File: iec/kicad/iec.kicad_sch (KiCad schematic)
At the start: 6 parts, among them J2 Conn_RIOT, J2 RESET, J3 DIN-6, U1 74LS06

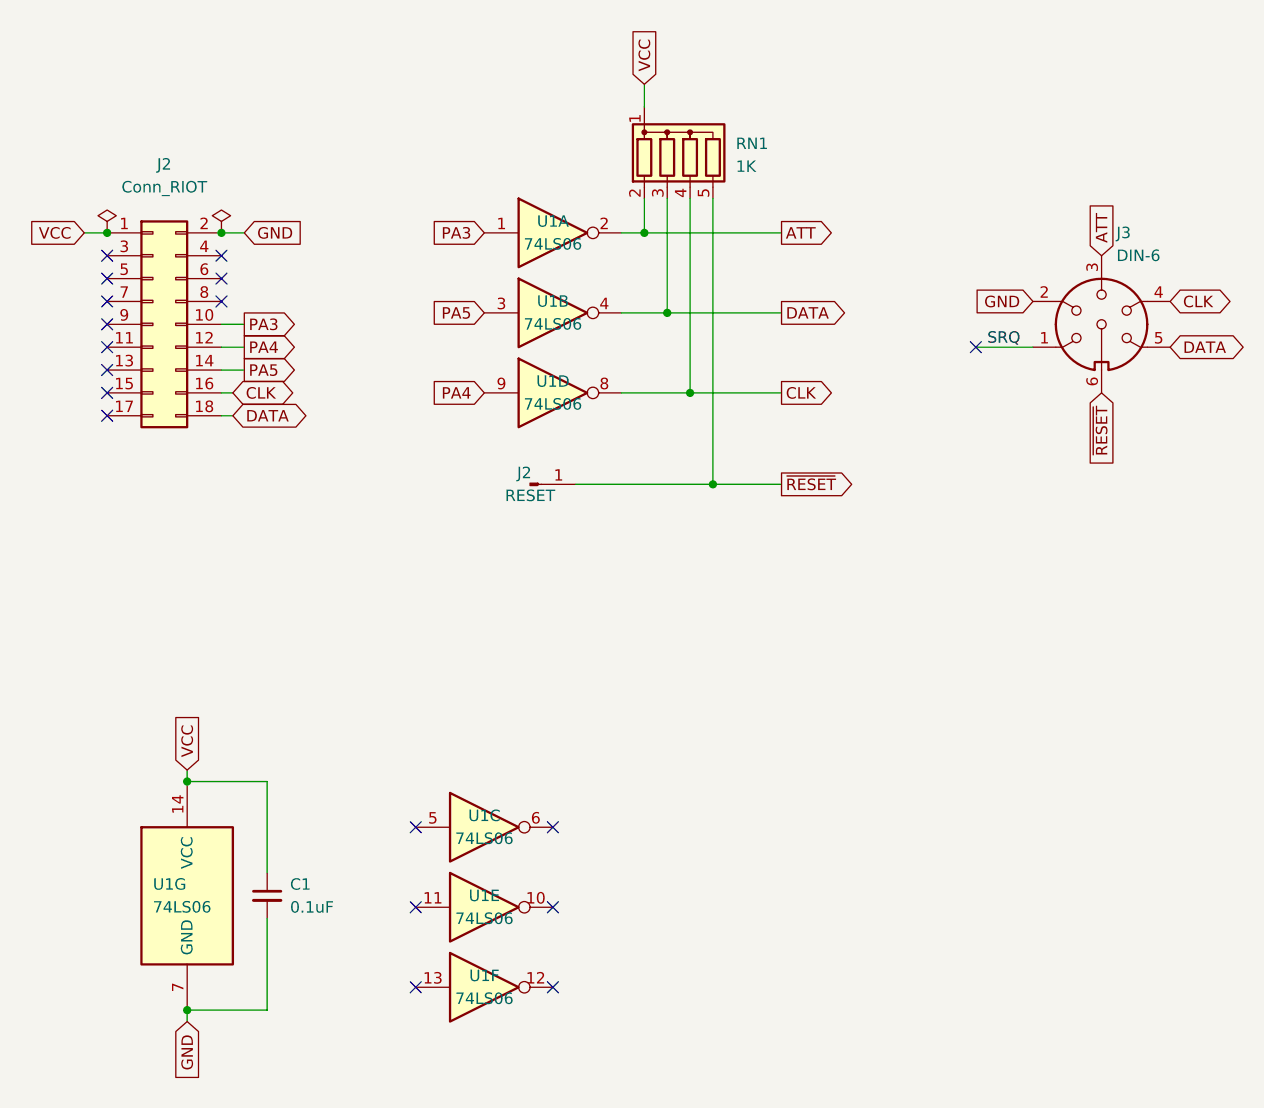
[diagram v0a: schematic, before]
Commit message: Expose VCC and GND via pins for SD2IEC devices
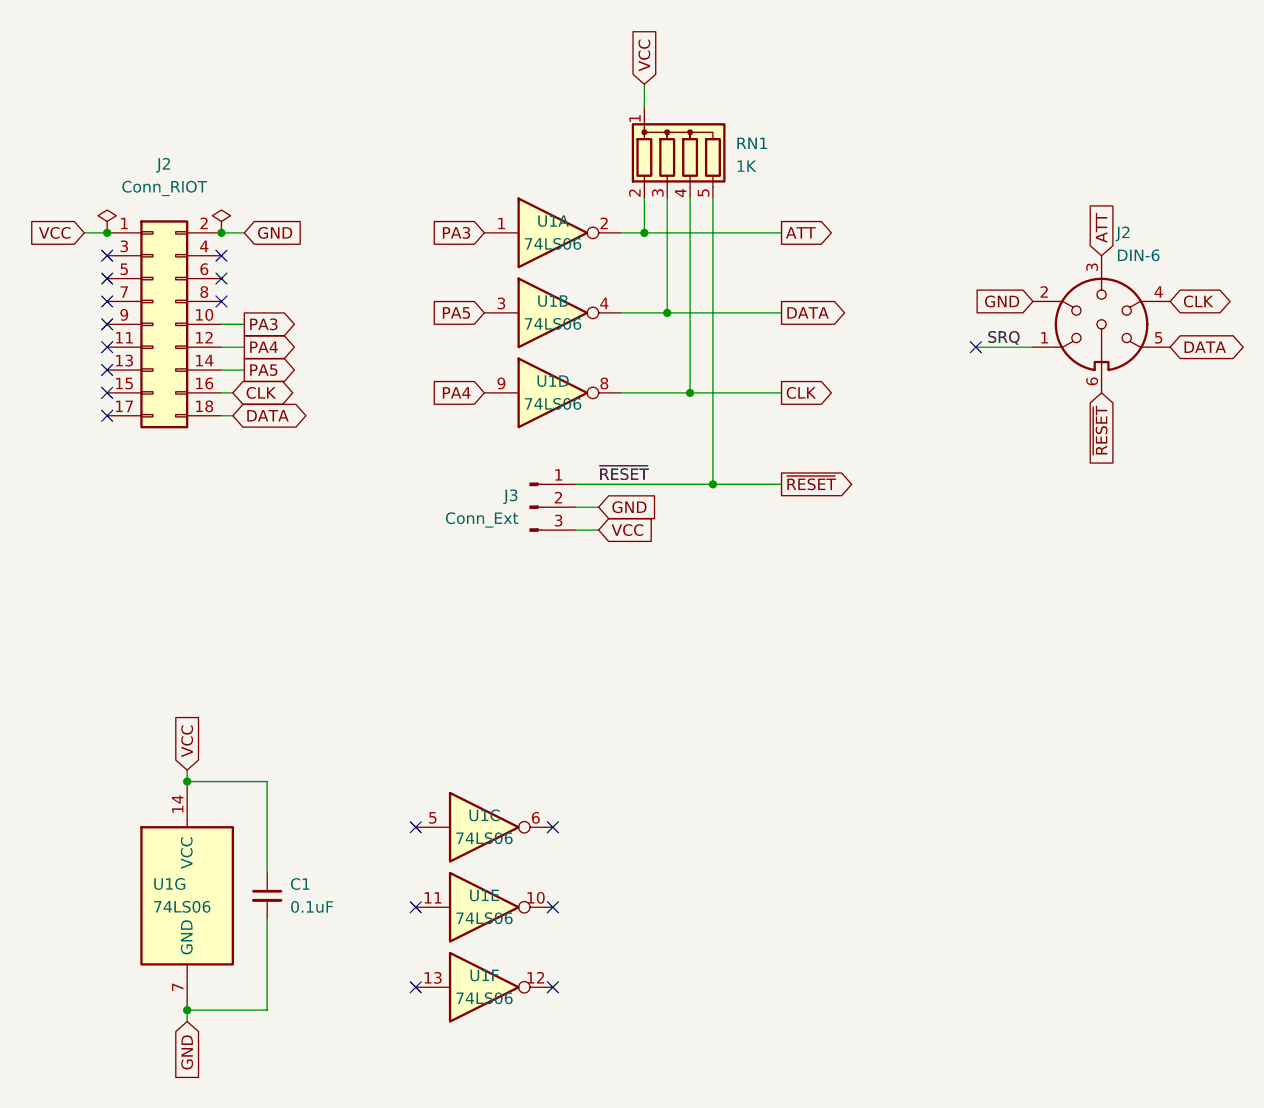
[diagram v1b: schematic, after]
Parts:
- removed J2: RESET, Connector_PinHeader_2.54mm:PinHeader_1x01_P2.54mm_Horizontal, symbol Connector:Conn_01x01_Pin
- added J3: Conn_Ext, Connector_PinHeader_2.54mm:PinHeader_1x03_P2.54mm_Vertical, symbol Connector:Conn_01x03_Pin
- renumbered J3 to J2
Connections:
- net GND: now also J3.2 (Pin_2)
- net VCC: now also J3.3 (Pin_3)
- net ~{RESET}: now also J3.1 (Pin_1)
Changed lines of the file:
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@@
+    (stroke (width 0) (type default))
+  )
+  (wire (pts (xy 151.13 102.87) (xy 148.59 102.87))
     (stroke (width 0) (type default))
   )
@@
     (stroke (width 0) (type default))
   )
+  (wire (pts (xy 151.13 105.41) (xy 148.59 105.41))
+    (stroke (width 0) (type default))
+  )
   (wire (pts (xy 105.41 133.35) (xy 114.3 133.35))
     (stroke (width 0) (type default))
+  )
+  (label "~{RESET}" (at 151.13 100.33 0) (fields_autoplaced)
+    (effects (font (size 1.27 1.27)) (justify left bottom))
   )
   (label "SRQ" (at 194.31 85.09 0) (fields_autoplaced)
@@
     )
   )
+  (global_label "VCC" (shape input) (at 151.13 105.41 0) (fields_autoplaced)
+    (effects (font (size 1.27 1.27)) (justify left))
+    (property "Intersheetrefs" "${INTERSHEET_REFS}" (at 157.6644 105.41 0)
+      (effects (font (size 1.27 1.27)) (justify left) hide)
+    )
+  )
   (global_label "PA4" (shape output) (at 111.76 85.09 0) (fields_autoplaced)
     (effects (font (size 1.27 1.27)) (justify left))
@@
     )
   )
+  (global_label "GND" (shape input) (at 151.13 102.87 0) (fields_autoplaced)
+    (effects (font (size 1.27 1.27)) (justify left))
+    (property "Intersheetrefs" "${INTERSHEET_REFS}" (at 157.9063 102.87 0)
+      (effects (font (size 1.27 1.27)) (justify left) hide)
+    )
+  )
   (symbol (lib_id "Connector:DIN-6") (at 207.01 82.55 0) (unit 1)
     (in_bom yes) (on_board yes) (dnp no) (fields_autoplaced)
-    (property "Reference" "J3" (at 208.6611 72.39 0)
+    (property "Reference" "J2" (at 208.6611 72.39 0)
       (effects (font (size 1.27 1.27)) (justify left))
     )
@@
     (pin "5")
     (pin "6")
-    (instances
-      (project "iec"
-        (path "/c75a3d49-44a2-4d4d-826f-a38b35ab1c9a"
-          (reference "J3") (unit 1)
-        )
-      )
-    )
-  )
-  (symbol (lib_id "Connector:Conn_01x01_Pin") (at 143.51 100.33 0) (unit 1)
-    (in_bom yes) (on_board yes) (dnp no)
-    (property "Reference" "J2" (at 142.875 99.06 0)
-      (effects (font (size 1.27 1.27)))
-    )
-    (property "Value" "RESET" (at 143.51 101.6 0)
-      (effects (font (size 1.27 1.27)))
-    )
-    (property "Footprint" "Connector_PinHeader_2.54mm:PinHeader_1x01_P2.54mm_Horizontal" (at 143.51 100.33 0)
-      (effects (font (size 1.27 1.27)) hide)
-    )
-    (property "Datasheet" "~" (at 143.51 100.33 0)
-      (effects (font (size 1.27 1.27)) hide)
-    )
-    (pin "1")
     (instances
       (project "iec"
@@
         )
       )
+    )
+  )
+  (symbol (lib_id "Connector:Conn_01x03_Pin") (at 143.51 102.87 0) (unit 1)
+    (in_bom yes) (on_board yes) (dnp no)
+    (property "Reference" "J3" (at 142.24 101.6 0)
+      (effects (font (size 1.27 1.27)) (justify right))
+    )
+    (property "Value" "Conn_Ext" (at 142.24 104.14 0)
+      (effects (font (size 1.27 1.27)) (justify right))
+    )
+    (property "Footprint" "Connector_PinHeader_2.54mm:PinHeader_1x03_P2.54mm_Vertical" (at 143.51 102.87 0)
+      (effects (font (size 1.27 1.27)) hide)
+    )
+    (property "Datasheet" "~" (at 143.51 102.87 0)
+      (effects (font (size 1.27 1.27)) hide)
+    )
+    (pin "1")
+    (pin "2")
+    (pin "3")
+    (instances
+      (project "iec"
+        (path "/c75a3d49-44a2-4d4d-826f-a38b35ab1c9a"
+          (reference "J3") (unit 1)
+        )
+      )
